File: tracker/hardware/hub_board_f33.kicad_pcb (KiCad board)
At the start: 2 copper layers, 75 x 55 mm, 14 parts, among them J1 SMA-868, J2 SMA-2G4, J3 SOLAR, U1 RP2040-Zero, U2 LoRa2021F33-2G4, U3 MAX-M10S, U4 MS5611, U5 TPS7A02

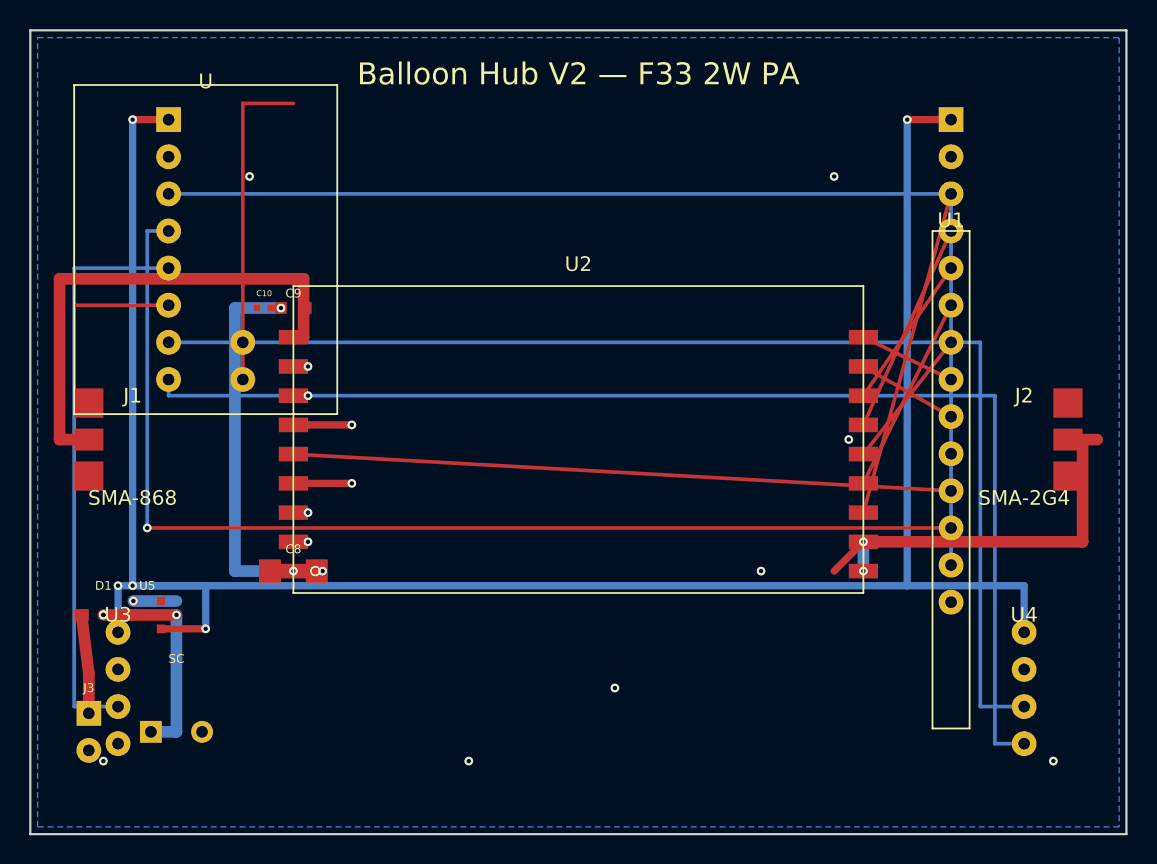
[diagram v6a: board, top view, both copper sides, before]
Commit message: fix(pcb): F33 surgical short fixes — C8 move, lane shifts, CE/GND/RF reroutes — shorts 15→16 (SPI rt.connect remains)
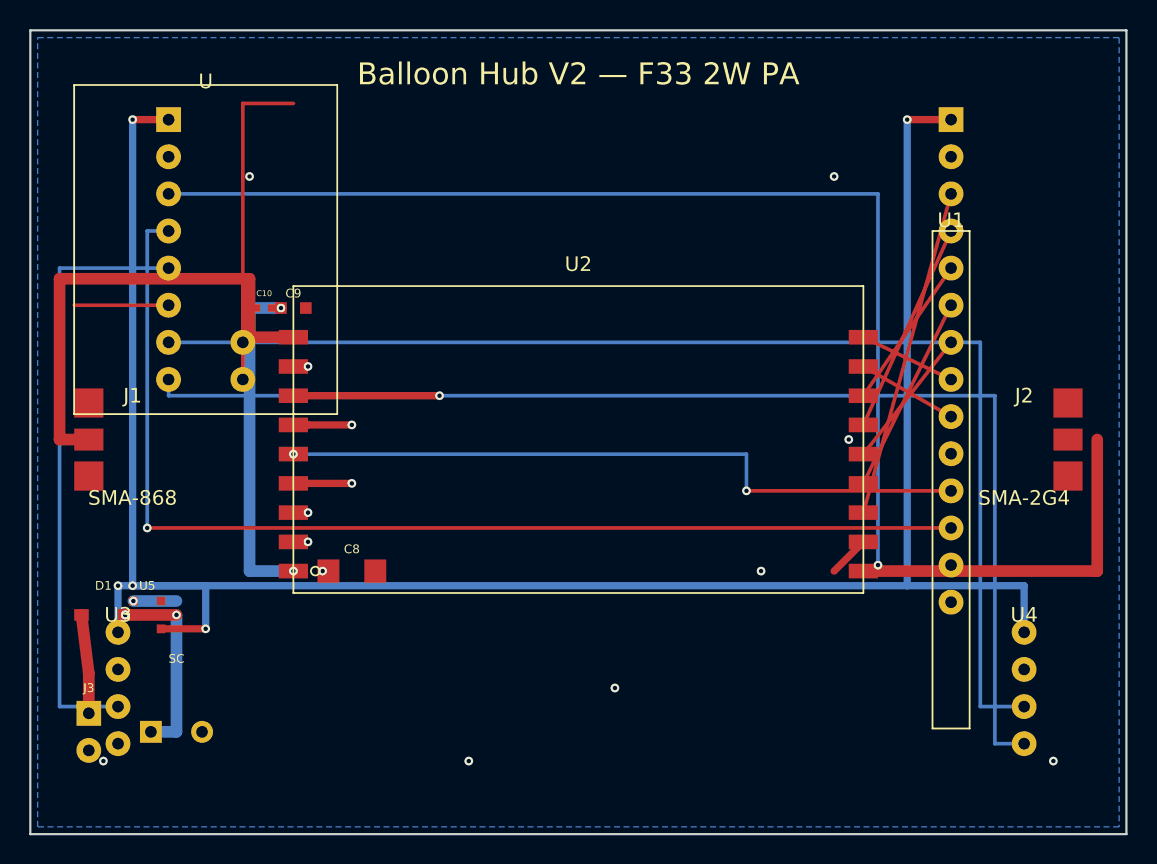
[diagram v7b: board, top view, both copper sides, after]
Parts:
- moved C8 4.00 mm to (22.0, 37.0)
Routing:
- net GND: track 14.8 -> 23.8 mm
- net ESP_TX_RP2040_RX: track 78.9 -> 73.9 mm
- net VCAP: track 42.9 -> 39.4 mm
- net LR2021_CE: track 45.1 -> 47.5 mm, vias 0 -> 2
- net GPS_TX_ESP_RX: track 39.5 -> 41.5 mm
- net RF_SUB_868: track 34.4 -> 33.0 mm
- net RF_2G4_2400: vias 2 -> 0
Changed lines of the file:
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@@
   )
   (footprint "Capacitor_SMD:C_1206_3216Metric" (layer "F.Cu")
-    (at 18 37)
+  (at 22 37)
     (property "Reference" "C8" (at 0 -1.5) (layer "F.SilkS") (effects (font (size 0.6 0.6) (thickness 0.1))))
     (property "Value" "100uF" (at 0 1.5) (layer "F.Fab") (effects (font (size 0.6 0.6) (thickness 0.1))))
@@
   (segment (start 4.0000 46.7300) (end 4.0000 44.0000) (width 0.8) (layer "F.Cu") (net 22))
   (segment (start 4.0000 44.0000) (end 3.5000 40.0000) (width 0.8) (layer "F.Cu") (net 22))
-  (segment (start 5.0000 40.0000) (end 10.0000 40.0000) (width 0.8) (layer "F.Cu") (net 21))
+  (segment (start 6.5000 40.0000) (end 10.0000 40.0000) (width 0.8) (layer "F.Cu") (net 21))
   (segment (start 7.0500 39.0500) (end 10.0000 39.0500) (width 0.8) (layer "B.Cu") (net 21))
   (segment (start 10.0000 40.0000) (end 10.0000 48.0000) (width 0.8) (layer "B.Cu") (net 21))
   (segment (start 10.0000 48.0000) (end 8.2500 48.0000) (width 0.8) (layer "B.Cu") (net 21))
-  (segment (start 18.0000 37.0000) (end 14.0000 37.0000) (width 0.8) (layer "B.Cu") (net 21))
-  (segment (start 14.0000 37.0000) (end 14.0000 19.0000) (width 0.8) (layer "B.Cu") (net 21))
-  (segment (start 14.0000 19.0000) (end 17.1500 19.0000) (width 0.8) (layer "B.Cu") (net 21))
+  (segment (start 18.0000 37.0000) (end 15.0000 37.0000) (width 0.8) (layer "B.Cu") (net 21))
+  (segment (start 15.0000 37.0000) (end 15.0000 19.0000) (width 0.8) (layer "B.Cu") (net 21))
+  (segment (start 15.0000 19.0000) (end 17.1500 19.0000) (width 0.8) (layer "B.Cu") (net 21))
   (segment (start 18.0000 35.0000) (end 19.0000 35.0000) (width 0.5) (layer "F.Cu") (net 2))
   (segment (start 18.0000 33.0000) (end 19.0000 33.0000) (width 0.5) (layer "F.Cu") (net 2))
@@
   (segment (start 19.0000 31.0000) (end 22.0000 31.0000) (width 0.5) (layer "F.Cu") (net 2))
   (segment (start 19.0000 27.0000) (end 22.0000 27.0000) (width 0.5) (layer "F.Cu") (net 2))
+  (segment (start 19.0000 25.0000) (end 28.0000 25.0000) (width 0.5) (layer "F.Cu") (net 2))
   (segment (start 57.0000 35.0000) (end 55.0000 37.0000) (width 0.5) (layer "F.Cu") (net 2))
-  (segment (start 18.0000 29.0000) (end 63.0000 31.5100) (width 0.25) (layer "F.Cu") (net 10))
-  (segment (start 18.0000 21.0000) (end 18.7000 21.0000) (width 0.8) (layer "F.Cu") (net 13))
-  (segment (start 18.7000 21.0000) (end 18.7000 17.0000) (width 0.8) (layer "F.Cu") (net 13))
-  (segment (start 18.7000 17.0000) (end 18.0000 17.0000) (width 0.8) (layer "F.Cu") (net 13))
-  (segment (start 18.0000 17.0000) (end 2.0000 17.0000) (width 0.8) (layer "F.Cu") (net 13))
+  (segment (start 18.0000 29.0000) (end 49.0000 29.0000) (width 0.25) (layer "B.Cu") (net 10))
+  (segment (start 49.0000 29.0000) (end 49.0000 31.5100) (width 0.25) (layer "B.Cu") (net 10))
+  (segment (start 49.0000 31.5100) (end 63.0000 31.5100) (width 0.25) (layer "F.Cu") (net 10))
+  (segment (start 18.0000 21.0000) (end 15.0000 21.0000) (width 0.8) (layer "F.Cu") (net 13))
+  (segment (start 15.0000 21.0000) (end 15.0000 17.0000) (width 0.8) (layer "F.Cu") (net 13))
+  (segment (start 15.0000 17.0000) (end 2.0000 17.0000) (width 0.8) (layer "F.Cu") (net 13))
   (segment (start 2.0000 17.0000) (end 2.0000 28.0000) (width 0.8) (layer "F.Cu") (net 13))
   (segment (start 2.0000 28.0000) (end 4.0000 28.0000) (width 0.8) (layer "F.Cu") (net 13))
-  (segment (start 57.0000 37.0000) (end 57.0000 35.0000) (width 0.8) (layer "B.Cu") (net 14))
-  (segment (start 57.0000 35.0000) (end 72.0000 35.0000) (width 0.8) (layer "F.Cu") (net 14))
-  (segment (start 72.0000 35.0000) (end 72.0000 28.0000) (width 0.8) (layer "F.Cu") (net 14))
-  (segment (start 72.0000 28.0000) (end 73.0000 28.0000) (width 0.8) (layer "F.Cu") (net 14))
+  (segment (start 57.0000 37.0000) (end 73.0000 37.0000) (width 0.8) (layer "F.Cu") (net 14))
+  (segment (start 73.0000 37.0000) (end 73.0000 28.0000) (width 0.8) (layer "F.Cu") (net 14))
   (segment (start 57.0000 33.0000) (end 63.0000 11.1900) (width 0.25) (layer "F.Cu") (net 3))
   (segment (start 57.0000 31.0000) (end 63.0000 18.8100) (width 0.25) (layer "F.Cu") (net 6))
@@
   (segment (start 57.0000 23.0000) (end 63.0000 26.4300) (width 0.25) (layer "F.Cu") (net 8))
   (segment (start 57.0000 21.0000) (end 63.0000 23.8900) (width 0.25) (layer "F.Cu") (net 9))
-  (segment (start 9.4600 11.1900) (end 63.0000 11.1900) (width 0.25) (layer "B.Cu") (net 15))
-  (segment (start 63.0000 11.1900) (end 63.0000 36.5900) (width 0.25) (layer "B.Cu") (net 15))
+  (segment (start 9.4600 11.1900) (end 58.0000 11.1900) (width 0.25) (layer "B.Cu") (net 15))
+  (segment (start 58.0000 11.1900) (end 58.0000 36.5900) (width 0.25) (layer "B.Cu") (net 15))
   (segment (start 63.0000 34.0500) (end 8.0000 34.0500) (width 0.25) (layer "F.Cu") (net 16))
   (segment (start 8.0000 34.0500) (end 8.0000 13.7300) (width 0.25) (layer "B.Cu") (net 16))
   (segment (start 8.0000 13.7300) (end 9.4600 13.7300) (width 0.25) (layer "B.Cu") (net 16))
-  (segment (start 6.0000 46.2700) (end 3.0000 46.2700) (width 0.25) (layer "B.Cu") (net 17))
-  (segment (start 3.0000 46.2700) (end 3.0000 16.2700) (width 0.25) (layer "B.Cu") (net 17))
-  (segment (start 3.0000 16.2700) (end 9.4600 16.2700) (width 0.25) (layer "B.Cu") (net 17))
+  (segment (start 6.0000 46.2700) (end 2.0000 46.2700) (width 0.25) (layer "B.Cu") (net 17))
+  (segment (start 2.0000 46.2700) (end 2.0000 16.2700) (width 0.25) (layer "B.Cu") (net 17))
+  (segment (start 2.0000 16.2700) (end 9.4600 16.2700) (width 0.25) (layer "B.Cu") (net 17))
   (segment (start 9.4600 21.3500) (end 65.0000 21.3500) (width 0.25) (layer "B.Cu") (net 11))
   (segment (start 65.0000 21.3500) (end 65.0000 46.2700) (width 0.25) (layer "B.Cu") (net 11))
@@
   (via (at 6.0000 41.1900) (size 0.6) (drill 0.3) (layers "F.Cu" "B.Cu") (net 1))
   (via (at 68.0000 41.1900) (size 0.6) (drill 0.3) (layers "F.Cu" "B.Cu") (net 1))
-  (via (at 5.0000 40.0000) (size 0.6) (drill 0.3) (layers "F.Cu" "B.Cu") (net 21))
-  (via (at 5.0000 40.0000) (size 0.6) (drill 0.3) (layers "F.Cu" "B.Cu") (net 21))
+  (via (at 6.5000 40.0000) (size 0.6) (drill 0.3) (layers "F.Cu" "B.Cu") (net 21))
+  (via (at 6.5000 40.0000) (size 0.6) (drill 0.3) (layers "F.Cu" "B.Cu") (net 21))
   (via (at 10.0000 40.0000) (size 0.6) (drill 0.3) (layers "F.Cu" "B.Cu") (net 21))
   (via (at 7.0500 39.0500) (size 0.6) (drill 0.3) (layers "F.Cu" "B.Cu") (net 21))
@@
   (via (at 22.0000 31.0000) (size 0.6) (drill 0.3) (layers "F.Cu" "B.Cu") (net 2))
   (via (at 22.0000 27.0000) (size 0.6) (drill 0.3) (layers "F.Cu" "B.Cu") (net 2))
-  (via (at 19.0000 25.0000) (size 0.6) (drill 0.3) (layers "F.Cu" "B.Cu") (net 2))
+  (via (at 28.0000 25.0000) (size 0.6) (drill 0.3) (layers "F.Cu" "B.Cu") (net 2))
   (via (at 19.0000 23.0000) (size 0.6) (drill 0.3) (layers "F.Cu" "B.Cu") (net 2))
   (via (at 56.0000 28.0000) (size 0.6) (drill 0.3) (layers "F.Cu" "B.Cu") (net 2))
   (via (at 20.0000 37.0000) (size 0.6) (drill 0.3) (layers "F.Cu" "B.Cu") (net 2))
   (via (at 50.0000 37.0000) (size 0.6) (drill 0.3) (layers "F.Cu" "B.Cu") (net 2))
-  (via (at 57.0000 37.0000) (size 0.6) (drill 0.3) (layers "F.Cu" "B.Cu") (net 14))
-  (via (at 57.0000 35.0000) (size 0.6) (drill 0.3) (layers "F.Cu" "B.Cu") (net 14))
+  (via (at 18.0000 29.0000) (size 0.6) (drill 0.3) (layers "F.Cu" "B.Cu") (net 10))
+  (via (at 49.0000 31.5100) (size 0.6) (drill 0.3) (layers "F.Cu" "B.Cu") (net 10))
   (via (at 9.4600 11.1900) (size 0.6) (drill 0.3) (layers "F.Cu" "B.Cu") (net 15))
-  (via (at 63.0000 36.5900) (size 0.6) (drill 0.3) (layers "F.Cu" "B.Cu") (net 15))
+  (via (at 58.0000 36.5900) (size 0.6) (drill 0.3) (layers "F.Cu" "B.Cu") (net 15))
   (via (at 63.0000 34.0500) (size 0.6) (drill 0.3) (layers "F.Cu" "B.Cu") (net 16))
   (via (at 63.0000 34.0500) (size 0.6) (drill 0.3) (layers "F.Cu" "B.Cu") (net 16))

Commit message: fix(pcb): F33 v6/v7 DRC reports + PCB updates — 16 shorts remaining (SPI rt.connect + B.Cu congestion)
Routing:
- net GND: track 23.8 -> 12.0 mm, vias 15 -> 14
- net VCAP: vias 7 -> 5
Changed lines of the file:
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@@
   (segment (start 4.0000 46.7300) (end 4.0000 44.0000) (width 0.8) (layer "F.Cu") (net 22))
   (segment (start 4.0000 44.0000) (end 3.5000 40.0000) (width 0.8) (layer "F.Cu") (net 22))
-  (segment (start 6.5000 40.0000) (end 10.0000 40.0000) (width 0.8) (layer "F.Cu") (net 21))
+  (segment (start 6.5000 40.0000) (end 8.0000 40.0000) (width 0.8) (layer "F.Cu") (net 21))
+  (segment (start 8.0000 40.0000) (end 10.0000 40.0000) (width 0.8) (layer "B.Cu") (net 21))
   (segment (start 7.0500 39.0500) (end 10.0000 39.0500) (width 0.8) (layer "B.Cu") (net 21))
   (segment (start 10.0000 40.0000) (end 10.0000 48.0000) (width 0.8) (layer "B.Cu") (net 21))
@@
   (segment (start 19.0000 31.0000) (end 22.0000 31.0000) (width 0.5) (layer "F.Cu") (net 2))
   (segment (start 19.0000 27.0000) (end 22.0000 27.0000) (width 0.5) (layer "F.Cu") (net 2))
-  (segment (start 19.0000 25.0000) (end 28.0000 25.0000) (width 0.5) (layer "F.Cu") (net 2))
-  (segment (start 57.0000 35.0000) (end 55.0000 37.0000) (width 0.5) (layer "F.Cu") (net 2))
   (segment (start 18.0000 29.0000) (end 49.0000 29.0000) (width 0.25) (layer "B.Cu") (net 10))
   (segment (start 49.0000 29.0000) (end 49.0000 31.5100) (width 0.25) (layer "B.Cu") (net 10))
@@
   (via (at 6.0000 41.1900) (size 0.6) (drill 0.3) (layers "F.Cu" "B.Cu") (net 1))
   (via (at 68.0000 41.1900) (size 0.6) (drill 0.3) (layers "F.Cu" "B.Cu") (net 1))
-  (via (at 6.5000 40.0000) (size 0.6) (drill 0.3) (layers "F.Cu" "B.Cu") (net 21))
-  (via (at 6.5000 40.0000) (size 0.6) (drill 0.3) (layers "F.Cu" "B.Cu") (net 21))
-  (via (at 10.0000 40.0000) (size 0.6) (drill 0.3) (layers "F.Cu" "B.Cu") (net 21))
+  (via (at 8.0000 40.0000) (size 0.6) (drill 0.3) (layers "F.Cu" "B.Cu") (net 21))
   (via (at 7.0500 39.0500) (size 0.6) (drill 0.3) (layers "F.Cu" "B.Cu") (net 21))
   (via (at 8.2500 48.0000) (size 0.6) (drill 0.3) (layers "F.Cu" "B.Cu") (net 21))
@@
   (via (at 22.0000 31.0000) (size 0.6) (drill 0.3) (layers "F.Cu" "B.Cu") (net 2))
   (via (at 22.0000 27.0000) (size 0.6) (drill 0.3) (layers "F.Cu" "B.Cu") (net 2))
-  (via (at 28.0000 25.0000) (size 0.6) (drill 0.3) (layers "F.Cu" "B.Cu") (net 2))
   (via (at 19.0000 23.0000) (size 0.6) (drill 0.3) (layers "F.Cu" "B.Cu") (net 2))
   (via (at 56.0000 28.0000) (size 0.6) (drill 0.3) (layers "F.Cu" "B.Cu") (net 2))
